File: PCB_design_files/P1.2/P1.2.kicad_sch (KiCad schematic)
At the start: 46 parts, among them J1 EEG_IN-, J10 BAT+, J11 BOOST, J2 EEG_IN+, J3 +3.3V, J4 GND, J5 -3V3, J6 EEG_INPUT, J7 STAGE_1_OUT, J8 STAGE_2_OUT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

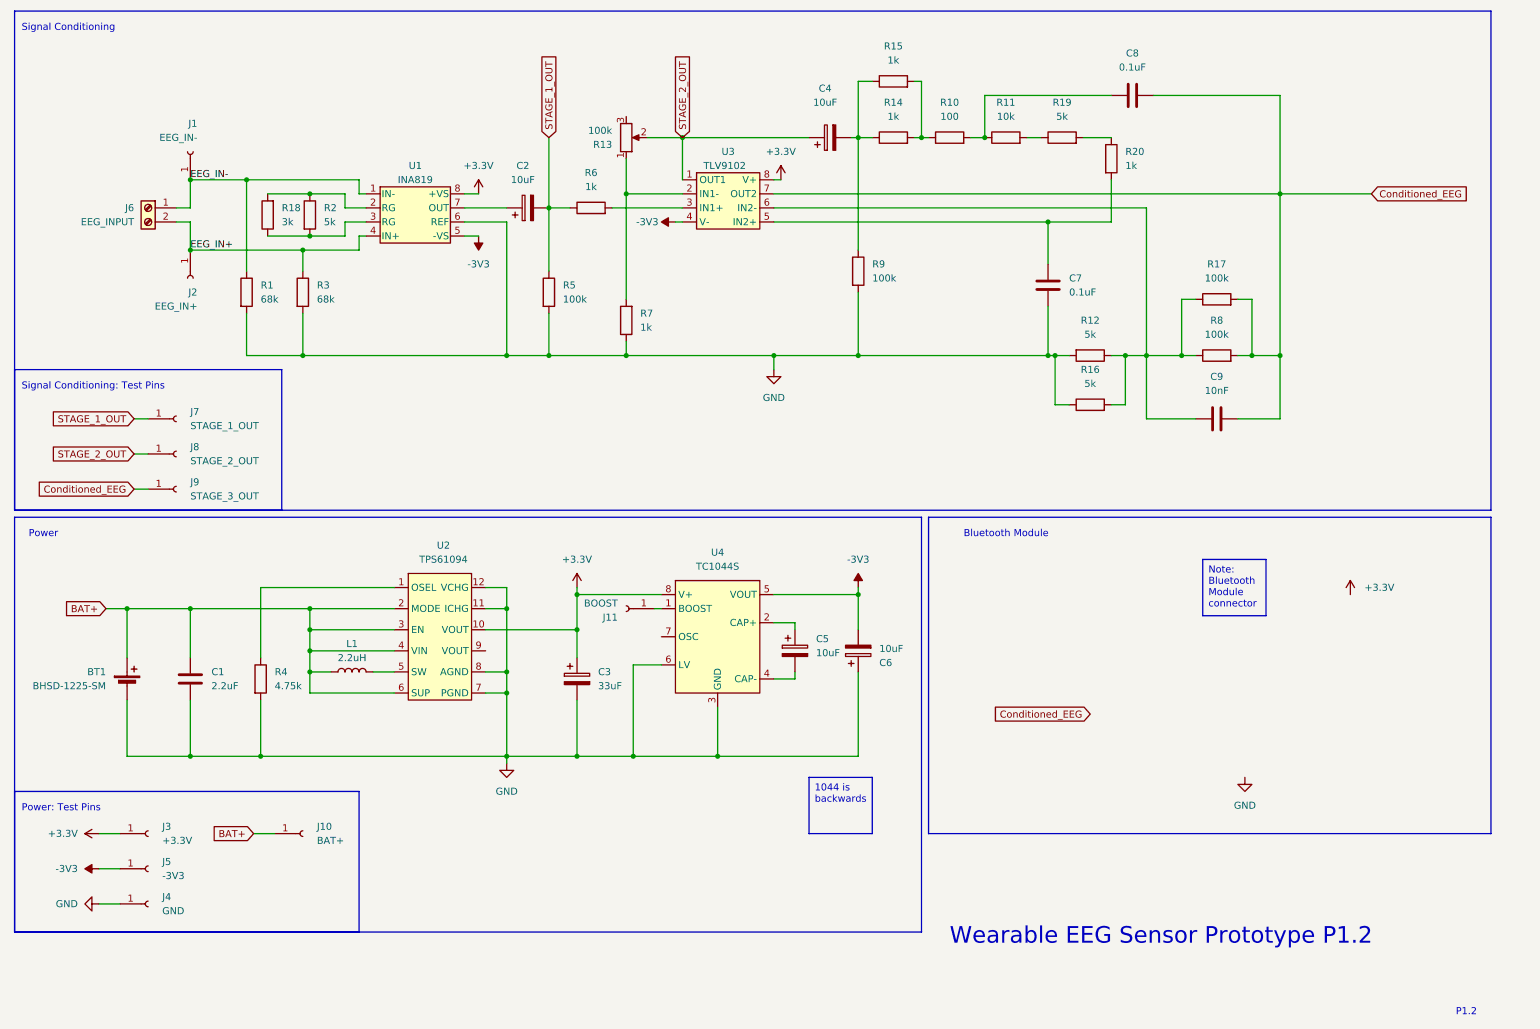
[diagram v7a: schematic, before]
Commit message: Updated schematic based on Nov.25 lab tests
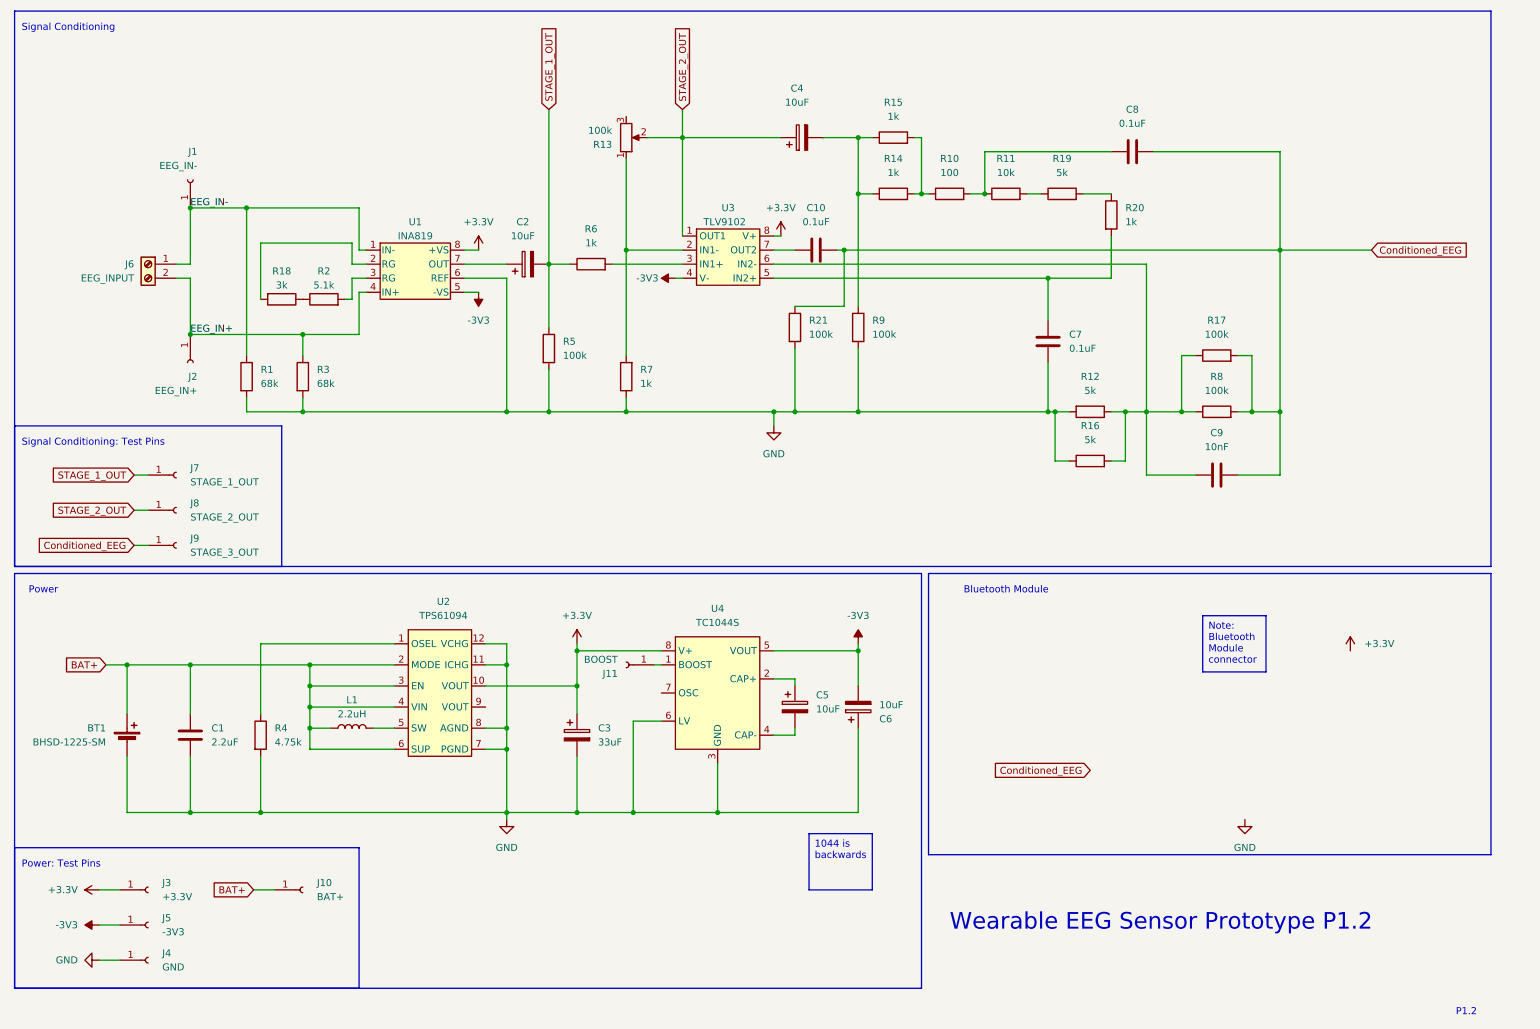
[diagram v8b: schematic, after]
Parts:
- added C10: 0.1uF, Capacitor_THT:C_Rect_L7.0mm_W4.5mm_P5.00mm, symbol Device:C
- added R21: 100k, Resistor_THT:R_Axial_DIN0207_L6.3mm_D2.5mm_P10.16mm_Horizontal, symbol Device:R
- R2: value 5k -> 5.1k
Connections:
- net Conditioned_EEG: now also C10.1, R21.1; no longer U3.7 (OUT2)
- net GND: now also R21.2
- net at R2.2, U1.3 (RG): no longer R18.1
- net at R18.2, U1.2 (RG): no longer R2.1
- new net: R18.1, R2.1
- new net: C10.2, U3.7 (OUT2)
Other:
- moved on the sheet: BT1, C1, C2, C3, C4, C5, C6, C7, C8, C9, J1, J10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
